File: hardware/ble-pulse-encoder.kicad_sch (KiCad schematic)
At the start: 55 parts, among them J1 USB_B_Micro, J2 EZmate-3, J3 EZmate-4, J4 TC2030-IDC-NL, J5 EZmate-5, Q1 BSS84, Q2 Q_Photo_NPN_CBE, Q3 Q_Photo_NPN_CBE, SW1 SW_Push, U1 STBC08, U2 nRF52832-QFxx, U3 MIC5301, Y1 32.768kHz, Y2 32MHz

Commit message: r0
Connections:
- net D0_PWR: now also U2.17 (P0.14); no longer U2.16 (P0.13)
- net D1_PWR: now also U2.18 (P0.15); no longer U2.19 (P0.16)
- net PH0_SENSE: now also U2.16 (P0.13); no longer U2.17 (P0.14)
- net PH1_PWR: now also U2.19 (P0.16); no longer U2.18 (P0.15)
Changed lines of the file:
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@@
     (effects (font (size 1.27 1.27)) (justify left bottom))
   )
+  (label "PH0_PWR" (at 139.7 116.84 180) (fields_autoplaced)
+    (effects (font (size 1.27 1.27)) (justify right bottom))
+  )
   (label "XL1" (at 139.7 86.36 180) (fields_autoplaced)
+    (effects (font (size 1.27 1.27)) (justify right bottom))
+  )
+  (label "D0_PWR" (at 139.7 121.92 180) (fields_autoplaced)
     (effects (font (size 1.27 1.27)) (justify right bottom))
   )
@@
     (effects (font (size 1.27 1.27)) (justify left bottom))
   )
-  (label "PH0_SENSE" (at 139.7 121.92 180) (fields_autoplaced)
-    (effects (font (size 1.27 1.27)) (justify right bottom))
-  )
   (label "LED_B" (at 220.98 121.92 0) (fields_autoplaced)
     (effects (font (size 1.27 1.27)) (justify left bottom))
@@
     (effects (font (size 1.27 1.27)) (justify left bottom))
   )
-  (label "PH1_PWR" (at 139.7 124.46 180) (fields_autoplaced)
+  (label "PH1_PWR" (at 139.7 127 180) (fields_autoplaced)
     (effects (font (size 1.27 1.27)) (justify right bottom))
   )
@@
   (label "NRF_SWDIO" (at 160.02 123.19 0) (fields_autoplaced)
     (effects (font (size 1.27 1.27)) (justify left bottom))
+  )
+  (label "PH0_SENSE" (at 139.7 119.38 180) (fields_autoplaced)
+    (effects (font (size 1.27 1.27)) (justify right bottom))
   )
   (label "SDA" (at 156.21 207.01 0) (fields_autoplaced)
@@
     (effects (font (size 1.27 1.27)) (justify left bottom))
   )
+  (label "D1_PWR" (at 139.7 124.46 180) (fields_autoplaced)
+    (effects (font (size 1.27 1.27)) (justify right bottom))
+  )
   (label "XL1" (at 48.26 152.4 180) (fields_autoplaced)
     (effects (font (size 1.27 1.27)) (justify right bottom))
@@
   )
   (label "SCL" (at 139.7 137.16 180) (fields_autoplaced)
-    (effects (font (size 1.27 1.27)) (justify right bottom))
-  )
-  (label "PH0_PWR" (at 139.7 116.84 180) (fields_autoplaced)
     (effects (font (size 1.27 1.27)) (justify right bottom))
   )
@@
     (effects (font (size 1.27 1.27)) (justify right bottom))
   )
-  (label "D1_PWR" (at 139.7 127 180) (fields_autoplaced)
-    (effects (font (size 1.27 1.27)) (justify right bottom))
-  )
   (label "LED_A" (at 139.7 154.94 180) (fields_autoplaced)
     (effects (font (size 1.27 1.27)) (justify right bottom))
   )
-  (label "D0_PWR" (at 139.7 119.38 180) (fields_autoplaced)
-    (effects (font (size 1.27 1.27)) (justify right bottom))
-  )

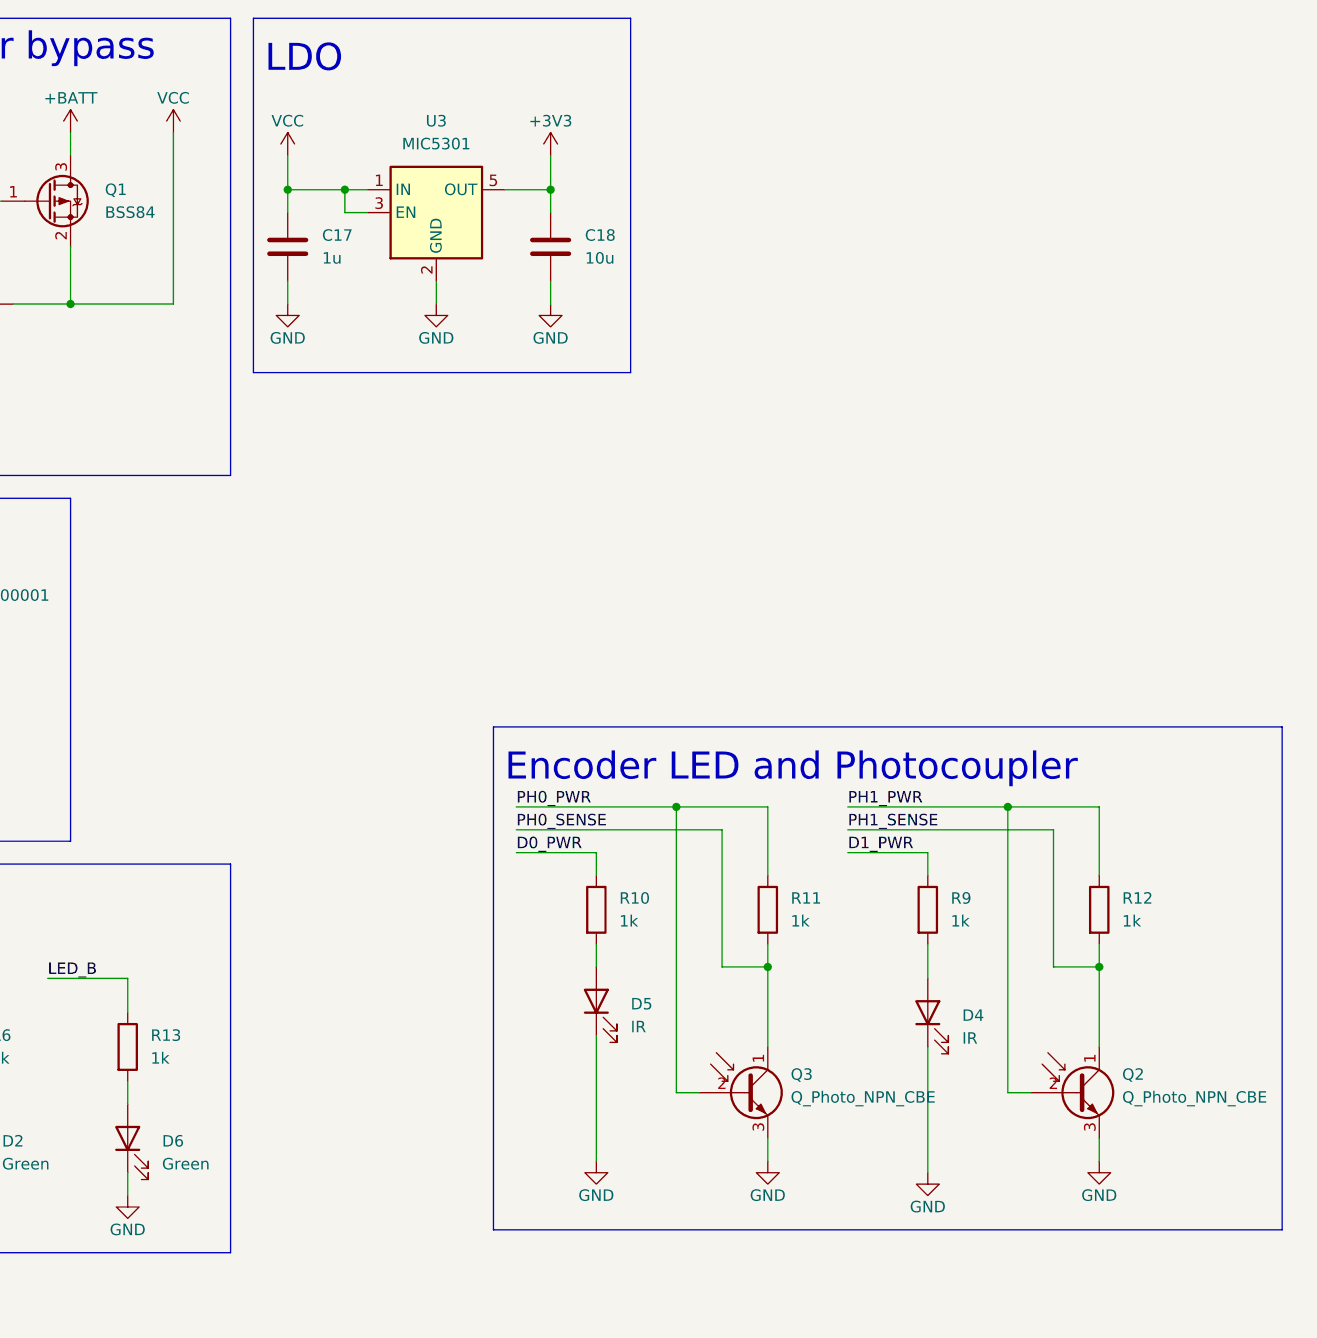
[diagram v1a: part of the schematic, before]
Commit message: hw: few p/n tweaks
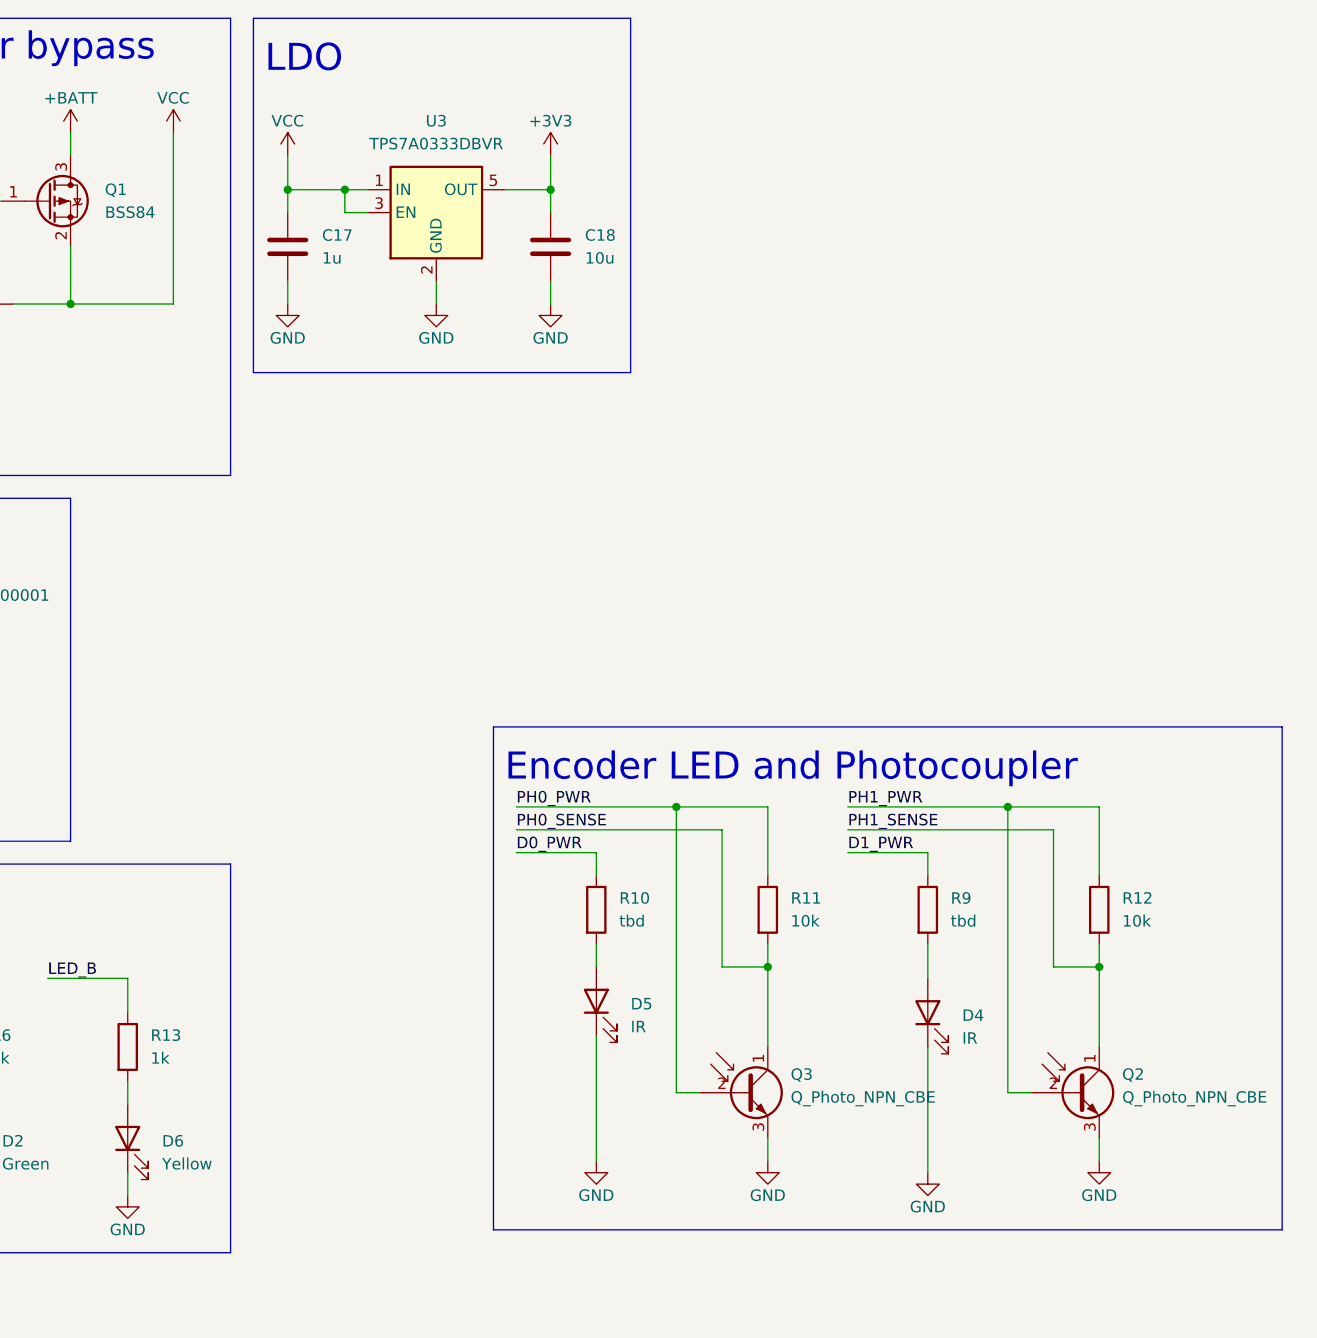
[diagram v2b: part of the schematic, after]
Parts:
- D6: value Green -> Yellow
- R10, R9: value 1k -> tbd
- R11, R12: value 1k -> 10k
- U3: value MIC5301 -> TPS7A0333DBVR
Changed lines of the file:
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@@
   (symbol (lib_id "Device:LED") (at 229.87 139.7 90) (unit 1)
     (in_bom yes) (on_board yes) (dnp no) (fields_autoplaced)
-    (property "Reference" "D6" (at 233.68 140.0174 90)
+    (property "Reference" "D6" (at 233.68 140.0175 90)
       (effects (font (size 1.27 1.27)) (justify right))
     )
-    (property "Value" "Green" (at 233.68 142.5574 90)
+    (property "Value" "Yellow" (at 233.68 142.5575 90)
       (effects (font (size 1.27 1.27)) (justify right))
     )
@@
       (effects (font (size 1.27 1.27)) (justify left))
     )
-    (property "Value" "1k" (at 340.36 115.57 0)
+    (property "Value" "10k" (at 340.36 115.57 0)
       (effects (font (size 1.27 1.27)) (justify left))
     )
@@
       (effects (font (size 1.27 1.27)))
     )
-    (property "Value" "MIC5301" (at 264.16 29.21 0)
+    (property "Value" "TPS7A0333DBVR" (at 264.16 29.21 0)
       (effects (font (size 1.27 1.27)))
     )
@@
       (effects (font (size 1.27 1.27)) hide)
     )
-    (property "Datasheet" "https://www.ti.com/lit/ds/symlink/tps7a05.pdf" (at 264.16 24.13 0)
+    (property "Datasheet" "https://www.ti.com/lit/ds/symlink/tps7a03.pdf" (at 264.16 24.13 0)
       (effects (font (size 1.27 1.27)) hide)
     )
@@
       (effects (font (size 1.27 1.27)) (justify left))
     )
-    (property "Value" "1k" (at 284.48 115.57 0)
+    (property "Value" "tbd" (at 284.48 115.57 0)
       (effects (font (size 1.27 1.27)) (justify left))
     )
@@
       (effects (font (size 1.27 1.27)) (justify left))
     )
-    (property "Value" "1k" (at 303.53 115.57 0)
+    (property "Value" "10k" (at 303.53 115.57 0)
       (effects (font (size 1.27 1.27)) (justify left))
     )
@@
       (effects (font (size 1.27 1.27)) (justify left))
     )
-    (property "Value" "1k" (at 321.31 115.57 0)
+    (property "Value" "tbd" (at 321.31 115.57 0)
       (effects (font (size 1.27 1.27)) (justify left))
     )

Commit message: hw: assembly notes
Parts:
- R10, R9: value tbd -> 470
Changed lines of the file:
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@@
       (effects (font (size 1.27 1.27)) (justify left))
     )
-    (property "Value" "tbd" (at 284.48 115.57 0)
+    (property "Value" "470" (at 284.48 115.57 0)
       (effects (font (size 1.27 1.27)) (justify left))
     )
@@
       (effects (font (size 1.27 1.27)) (justify left))
     )
-    (property "Value" "tbd" (at 321.31 115.57 0)
-      (effects (font (size 1.27 1.27)) (justify left))
-    )
+    (property "Value" "470" (at 321.31 115.57 0)
+      (effects (font (size 1.27 1.27)) (justify left))
+    )

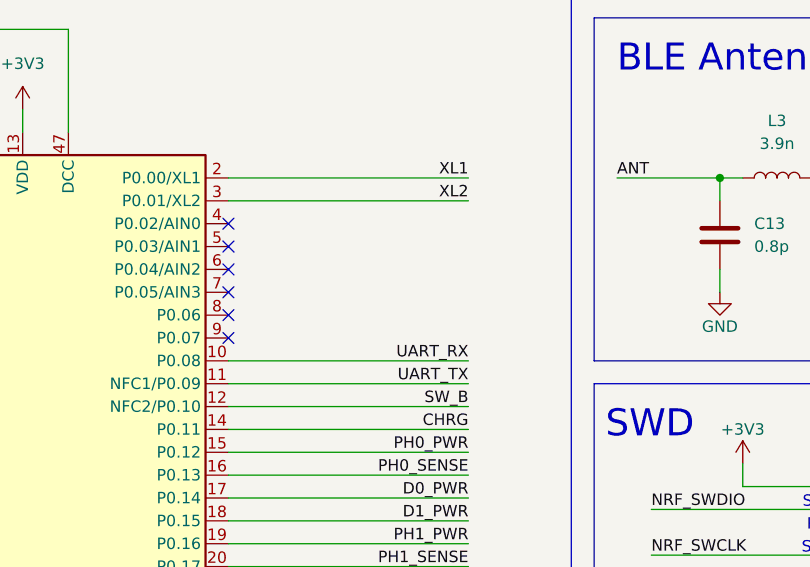
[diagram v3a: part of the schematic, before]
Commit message: hw: add note about missing vbatt line
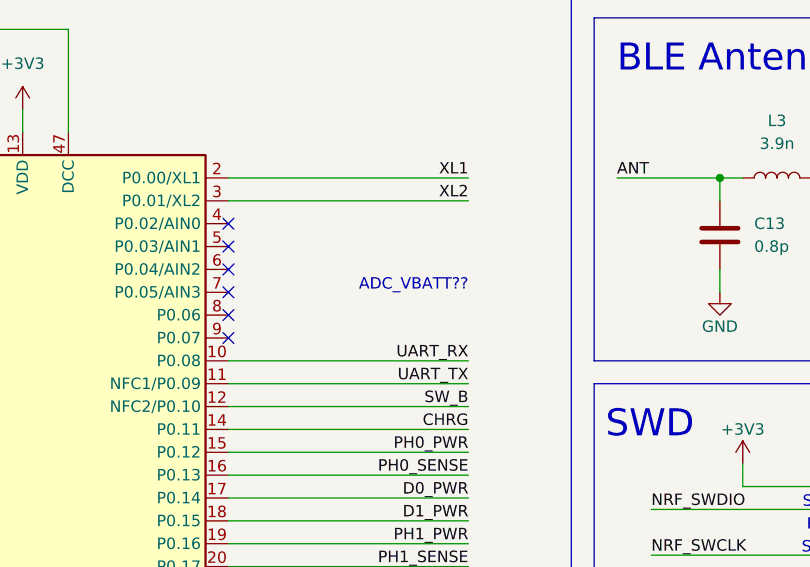
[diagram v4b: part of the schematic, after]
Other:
- note added: "ADC_VBATT??"
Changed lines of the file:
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@@
     (effects (font (size 3 3)) (justify left bottom))
+  )
+  (text "ADC_VBATT??" (at 139.7 99.06 0)
+    (effects (font (size 1.27 1.27)) (justify right bottom))
   )
   (text "nRF52832" (at 16.51 67.31 0)

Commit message: hw: r1
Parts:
- removed J1: USB_B_Micro, Connector_USB:USB_Micro-B_Amphenol_10104110_Horizontal, symbol Connector:USB_B_Micro
- removed J5: EZmate-5, balto:EZmate-5, symbol balto:EZmate-5
- removed Q2, Q3: Q_Photo_NPN_CBE, Connector_PinHeader_2.00mm:PinHeader_1x03_P2.00mm_Vertical, symbol Device:Q_Photo_NPN_CBE
- removed R7, R8: 4.7k, balto:R_0402_Worthington, symbol Device:R
- added J1: Conn_01x05, Connector_PinHeader_2.00mm:PinHeader_1x05_P2.00mm_Vertical, symbol Connector_Generic:Conn_01x05
- added J1: USB_C_Receptacle_USB2.0, Connector_USB:USB_C_Receptacle_JAE_DX07S016JA1R1500, symbol Connector:USB_C_Receptacle_USB2.0
- added R15, R16: 0, balto:R_0402_Worthington, symbol Device:R
- added R4, R5: 5.1k, balto:R_0402_Worthington, symbol Device:R
- AE1: footprint balto:2450AT18D0100001-R -> balto:2450AT18D0100001-L
- R11, R12: footprint Resistor_SMD:R_0603_1608Metric -> balto:R_0402_Worthington
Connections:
- net +5V: now also J1.A4 (VBUS), J1.A9 (VBUS), J1.B4 (VBUS), J1.B9 (VBUS)
- net ADC_VBATT: now also U2.7 (P0.05/AIN3)
- net GND: now also J1.3 (Pin_3), J1.5 (Pin_5), J1.A1 (GND), J1.A12 (GND), J1.B1 (GND), J1.B12 (GND), J1.S1 (SHIELD), R16.2, R4.2, R5.2
- net PH0_SENSE: now also J1.4 (Pin_4)
- net PH1_SENSE: now also J1.1 (Pin_1), R15.1
- net EXT_IRQ: no longer names the net of U2.21 (P0.18/SWO)
- net SCL: no longer names the net of U2.23 (P0.20)
- net SDA: no longer names the net of U2.22 (P0.19)
- new net: J1.A5 (CC1), R5.1
- new net: J1.2 (Pin_2), R15.2, R16.1
- new net: J1.B5 (CC2), R4.1
- no-connect marks 28 -> 31
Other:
- note added: "Encoder LED and Phototransistors"
- note added: "Phototransistor options: x A GND B x A GND X B GND ----------------- A A/GND GND B GND"
- note added: "USB"
- note removed: "ADC_VBATT??"
- note removed: "Encoder LED and Photocoupler"
- note removed: "Ext I2C"
- moved on the sheet: AE1, C1, C10, C11, C12, C13, C14, C15, C16, C17, C18, C2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

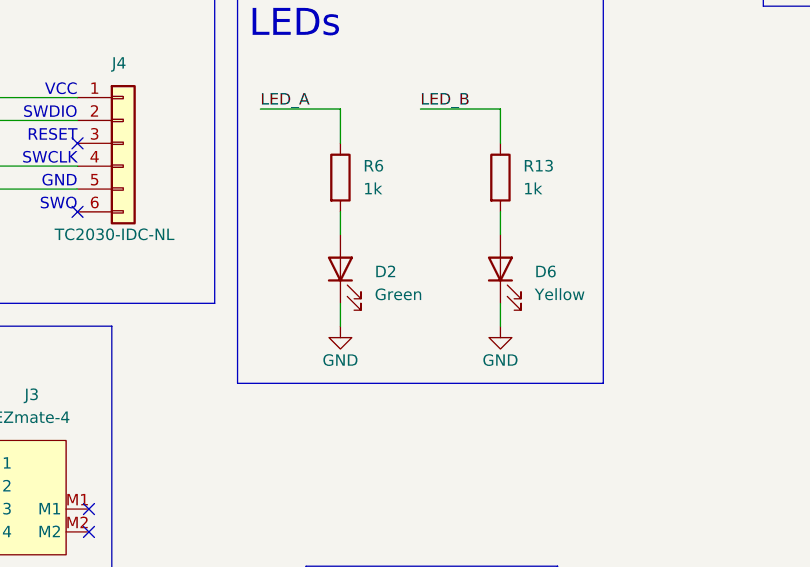
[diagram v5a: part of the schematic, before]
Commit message: hw: change D2 to blue
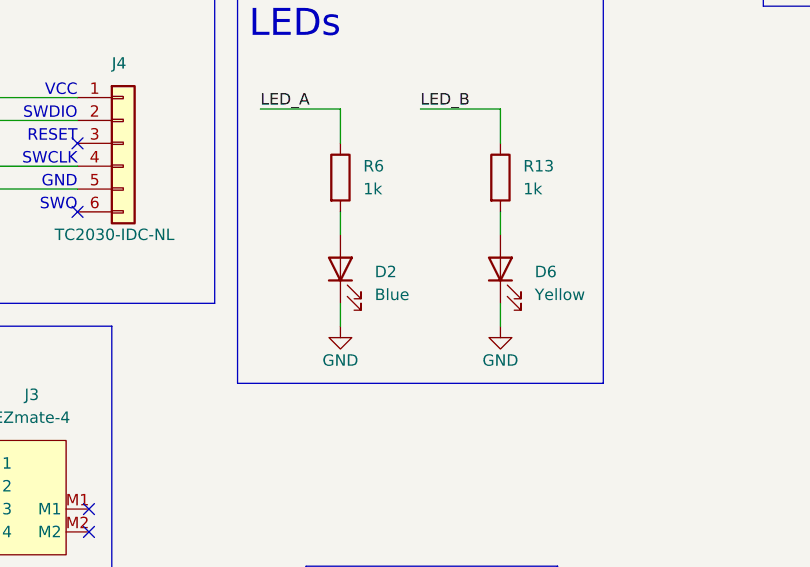
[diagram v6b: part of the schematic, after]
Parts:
- D2: value Green -> Blue
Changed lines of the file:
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@@
   (symbol (lib_id "Device:LED") (at 212.09 167.64 90) (unit 1)
     (in_bom yes) (on_board yes) (dnp no) (fields_autoplaced)
-    (property "Reference" "D2" (at 215.9 167.9574 90)
+    (property "Reference" "D2" (at 215.9 167.9575 90)
       (effects (font (size 1.27 1.27)) (justify right))
     )
-    (property "Value" "Green" (at 215.9 170.4974 90)
+    (property "Value" "Blue" (at 215.9 170.4975 90)
       (effects (font (size 1.27 1.27)) (justify right))
     )
